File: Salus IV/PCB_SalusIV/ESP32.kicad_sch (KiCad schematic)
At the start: 6 parts

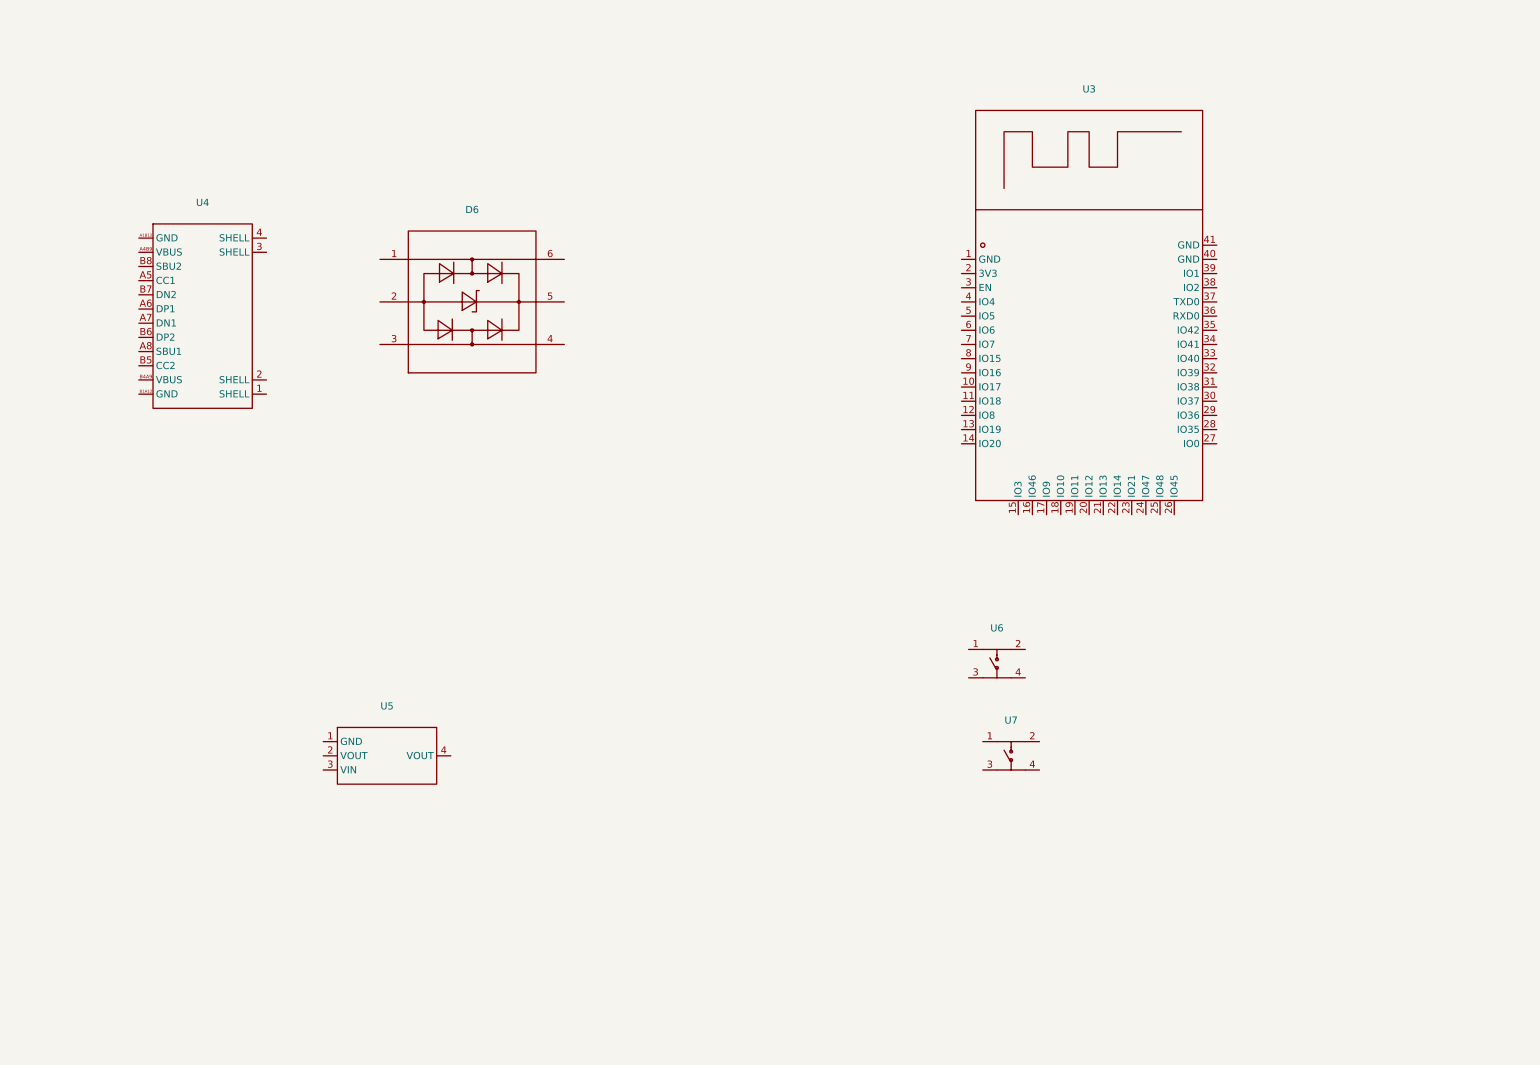
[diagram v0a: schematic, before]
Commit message: Se desarrollo el esquematico de la ESP32
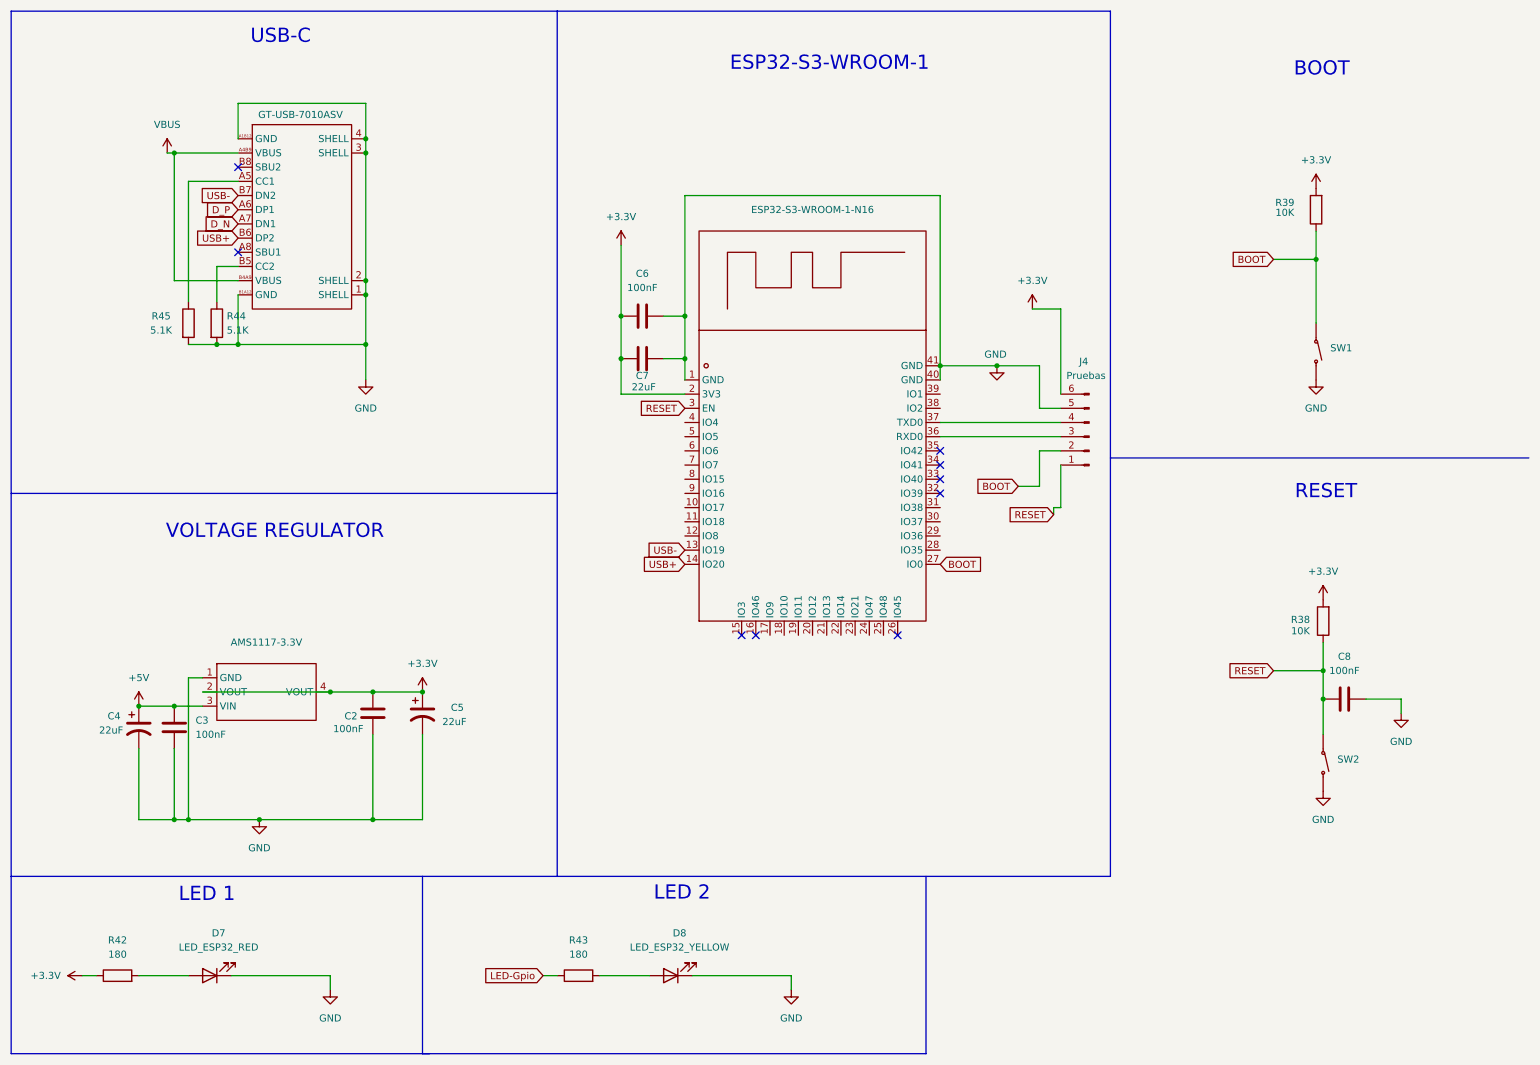
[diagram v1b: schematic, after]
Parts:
- removed D6: ~, Footprints:Protector-ESD, symbol Simbolos:USBLC6-2SC6
- removed U6, U7: ~, Footprints:Switch-Definitivo, symbol Simbolos:TPS645-5NC60
- added C2, C3, C6, C8: 100nF, Capacitor_SMD:C_0402_1005Metric, symbol Device:C
- added C4, C5: 22uF, Footprints:CASE-A_3216, symbol Device:C_Polarized_US
- added C7: 22uF, Capacitor_SMD:C_0402_1005Metric, symbol Device:C
- added D7: LED_ESP32_RED, LED_SMD:LED_0603_1608Metric, symbol Device:LED
- added D8: LED_ESP32_YELLOW, LED_SMD:LED_0603_1608Metric, symbol Device:LED
- added J4: Pruebas, Connector_PinHeader_2.54mm:PinHeader_1x06_P2.54mm_Vertical, symbol Connector:Conn_01x06_Pin
- added R38, R39: 10K, Resistor_SMD:R_1206_3216Metric, symbol Device:R
- added R42, R43: 180, Resistor_SMD:R_1206_3216Metric, symbol Device:R
- added R44, R45: 5.1K, Resistor_SMD:R_1206_3216Metric, symbol Device:R
- added SW1, SW2: ~, Footprints:Boton_Simple, symbol Simbolos:TS1201-TZ25HAM
- renumbered U5 to AMS1117-3.3V, U3 to ESP32-S3-WROOM-1-N16, U4 to GT-USB-7010ASV
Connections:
- net GND: now reaches GT-USB-7010ASV.1 (SHELL)
- net GND: now also AMS1117-3.3V.1 (GND), ESP32-S3-WROOM-1-N16.1 (GND), ESP32-S3-WROOM-1-N16.40 (GND), ESP32-S3-WROOM-1-N16.41 (GND), GT-USB-7010ASV.2 (SHELL), GT-USB-7010ASV.3 (SHELL), GT-USB-7010ASV.4 (SHELL), GT-USB-7010ASV.A1B12 (GND), GT-USB-7010ASV.B1A12 (GND), C2.2, C3.2, C4.2, C5.2, C6.2, C7.2, C8.2, D7.1 (K), D8.1 (K), J4.5 (Pin_5), R44.2, R45.2, SW1.2, SW2.2
- net VBUS: now reaches GT-USB-7010ASV.A4B9 (VBUS)
- net VBUS: now also GT-USB-7010ASV.B4A9 (VBUS)
- net at GT-USB-7010ASV.A5 (CC1): now also R45.1
- net D_P: now reaches GT-USB-7010ASV.A6 (DP1)
- net D_N: now reaches GT-USB-7010ASV.A7 (DN1)
- net at GT-USB-7010ASV.B5 (CC2): now also R44.1
- net USB+: now reaches GT-USB-7010ASV.B6 (DP2)
- net USB+: now also ESP32-S3-WROOM-1-N16.14 (IO20)
- net USB-: now reaches GT-USB-7010ASV.B7 (DN2)
- net USB-: now also ESP32-S3-WROOM-1-N16.13 (IO19)
- net +3.3V: now reaches ESP32-S3-WROOM-1-N16.2 (3V3)
- net +3.3V: now also AMS1117-3.3V.2 (VOUT), AMS1117-3.3V.4 (VOUT), C2.1, C5.1, C6.1, C7.1, J4.6 (Pin_6), R38.2, R39.2, R42.1
- net BOOT: now reaches ESP32-S3-WROOM-1-N16.27 (IO0)
- net BOOT: now also J4.2 (Pin_2), R39.1, SW1.1
- net RESET: now reaches ESP32-S3-WROOM-1-N16.3 (EN)
- net RESET: now also C8.1, J4.1 (Pin_1), R38.1, SW2.1
- net at ESP32-S3-WROOM-1-N16.36 (RXD0): now also J4.3 (Pin_3)
- net at ESP32-S3-WROOM-1-N16.37 (TXD0): now also J4.4 (Pin_4)
- net +5V: now reaches AMS1117-3.3V.3 (VIN)
- net +5V: now also C3.1, C4.1
- new net: D8.2 (A), R43.2
- new net: D7.2 (A), R42.2
- new net LED-Gpio: R43.1
- no-connect marks 0 -> 9
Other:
- note added: "BOOT"
- note added: "ESP32-S3-WROOM-1"
- note added: "LED 1"
- note added: "LED 2"
- note added: "RESET"
- note added: "USB-C"
- note added: "VOLTAGE REGULATOR"
- moved on the sheet: AMS1117-3.3V, ESP32-S3-WROOM-1-N16, GT-USB-7010ASV

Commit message: Se agregan cambios antes de agregar arrays
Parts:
- added J5: GPIO1-Libre, Connector_PinHeader_2.54mm:PinHeader_1x03_P2.54mm_Vertical, symbol Connector:Conn_01x03_Pin
- added J6: GPIO2-Libre, Connector_PinHeader_2.54mm:PinHeader_1x03_P2.54mm_Vertical, symbol Connector:Conn_01x03_Pin
- renumbered AMS1117-3.3V to AMS1117-3.3V1, GT-USB-7010ASV to GT-USB-7010ASV1
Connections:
- net D_N is gone; now on net USB-: GT-USB-7010ASV1.A7 (DN1)
- net D_P is gone; now on net USB+: GT-USB-7010ASV1.A6 (DP1)
- net +3.3V: now also J4.1 (Pin_1); no longer J4.6 (Pin_6)
- net +5V: now also J5.2 (Pin_2), J6.2 (Pin_2)
- net BOOT: now also J4.5 (Pin_5); no longer J4.2 (Pin_2)
- net GND: now also J4.6 (Pin_6), J5.1 (Pin_1), J6.1 (Pin_1); no longer J4.5 (Pin_5)
- net LED-Gpio: now also ESP32-S3-WROOM-1-N16.28 (IO35)
- net RESET: now also J4.2 (Pin_2); no longer J4.1 (Pin_1)
- net TX1: now reaches ESP32-S3-WROOM-1-N16.10 (IO17)
- net RX1: now reaches ESP32-S3-WROOM-1-N16.11 (IO18)
- net PPM: now reaches ESP32-S3-WROOM-1-N16.12 (IO8)
- net HALL-1: now reaches ESP32-S3-WROOM-1-N16.17 (IO9)
- net HALL-2: now reaches ESP32-S3-WROOM-1-N16.18 (IO10)
- net HALL-3: now reaches ESP32-S3-WROOM-1-N16.19 (IO11)
- net ENABLE: now reaches ESP32-S3-WROOM-1-N16.20 (IO12)
- net LPWM: now reaches ESP32-S3-WROOM-1-N16.21 (IO13)
- net RPWM: now reaches ESP32-S3-WROOM-1-N16.22 (IO14)
- net Servo2: now reaches ESP32-S3-WROOM-1-N16.23 (IO21)
- net Servo1: now reaches ESP32-S3-WROOM-1-N16.24 (IO47)
- net ACELERADOR: now reaches ESP32-S3-WROOM-1-N16.25 (IO48)
- net Cambio: now reaches ESP32-S3-WROOM-1-N16.29 (IO36)
- net Reversa: now reaches ESP32-S3-WROOM-1-N16.30 (IO37)
- net Arranque: now reaches ESP32-S3-WROOM-1-N16.31 (IO38)
- net GPIO2: now reaches ESP32-S3-WROOM-1-N16.38 (IO2)
- net GPIO2: now also J5.3 (Pin_3)
- net GPIO1: now reaches ESP32-S3-WROOM-1-N16.39 (IO1)
- net GPIO1: now also J6.3 (Pin_3)
- net SDA_Expansor: now reaches ESP32-S3-WROOM-1-N16.4 (IO4)
- net SCL_Expansor: now reaches ESP32-S3-WROOM-1-N16.5 (IO5)
- net SDA-MUX: now reaches ESP32-S3-WROOM-1-N16.6 (IO6)
- net SCL-MUX: now reaches ESP32-S3-WROOM-1-N16.7 (IO7)
- net ADC_ES: now reaches ESP32-S3-WROOM-1-N16.8 (IO15)
- net Control_Bat: now reaches ESP32-S3-WROOM-1-N16.9 (IO16)

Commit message: Se agrega terminada antes de modificaciones de mejora
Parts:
- added R16, R17: 4.7K, Resistor_SMD:R_1206_3216Metric, symbol Device:R
- C2, C3, C6, C8: footprint Capacitor_SMD:C_0402_1005Metric -> Capacitor_SMD:C_0603_1608Metric; LCSC PN C1525 -> C1590
- C7: footprint Capacitor_SMD:C_0402_1005Metric -> Capacitor_SMD:C_1206_3216Metric
- R44: LCSC PN (none) -> C26044
- U1: renamed from ESP32-S3-WROOM-1-N16; value ~ -> ESP32-S3-WROOM-1-N16
- U4: renamed from AMS1117-3.3V1; value ~ -> AMS
- renumbered GT-USB-7010ASV1 to J21
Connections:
- net +3.3V: now also R16.2, R17.2
- net ENABLE: now also U1.22 (IO14); no longer U1.20 (IO12)
- net RPWM: now also U1.20 (IO12); no longer U1.22 (IO14)
- net SCL-MUX: no longer names the net of U1.7 (IO7)
- net SCL_Expansor renamed SCL-Expansores
- net SCL-Expansores: now also R17.1
- net SDA-MUX: no longer names the net of U1.6 (IO6)
- net SDA_Expansor renamed SDA-Expansores
- net SDA-Expansores: now also R16.1
- no-connect marks 9 -> 11

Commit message: Se guarda la PCB Salus IV ya terminada, queda revision final antes de envio
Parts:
- removed J4: Pruebas, Connector_PinHeader_2.54mm:PinHeader_1x06_P2.54mm_Vertical, symbol Connector:Conn_01x06_Pin
- removed J5: GPIO1-Libre, Connector_PinHeader_2.54mm:PinHeader_1x03_P2.54mm_Vertical, symbol Connector:Conn_01x03_Pin
- removed J6: GPIO2-Libre, Connector_PinHeader_2.54mm:PinHeader_1x03_P2.54mm_Vertical, symbol Connector:Conn_01x03_Pin
- removed R38, R39: 10K, Resistor_SMD:R_1206_3216Metric, symbol Device:R
- removed R43: 180, Resistor_SMD:R_1206_3216Metric, symbol Device:R
- removed R44: 5.1K, Resistor_SMD:R_1206_3216Metric, symbol Device:R
- added J17: Pruebas, Connector_PinHeader_2.54mm:PinHeader_1x06_P2.54mm_Vertical, symbol Connector:Conn_01x06_Pin
- added J18: GPIO2-Libre, Connector_PinHeader_2.54mm:PinHeader_1x03_P2.54mm_Vertical, symbol Connector:Conn_01x03_Pin
- added J19: GPIO1-Libre, Connector_PinHeader_2.54mm:PinHeader_1x03_P2.54mm_Vertical, symbol Connector:Conn_01x03_Pin
- added R22, R23: 10K, Resistor_SMD:R_0603_1608Metric, symbol Device:R
- added R24: 180, Resistor_SMD:R_0603_1608Metric, symbol Device:R
- added R25: 5.1K, Resistor_SMD:R_0603_1608Metric, symbol Device:R
- R16, R17: footprint Resistor_SMD:R_1206_3216Metric -> Resistor_SMD:R_0603_1608Metric; LCSC PN C26043 -> C99782
- R27: renamed from R42; footprint Resistor_SMD:R_1206_3216Metric -> Resistor_SMD:R_0603_1608Metric; LCSC PN C25356 -> C4316945
- R28: renamed from R45; footprint Resistor_SMD:R_1206_3216Metric -> Resistor_SMD:R_0603_1608Metric; LCSC PN C26044 -> C14677
- renumbered J21 to J16
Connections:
- net +3.3V: now also R16.1, R17.1, J17.1 (Pin_1), R22.2, R23.2; no longer R16.2, R17.2
- net +5V: now also J18.2 (Pin_2), J19.2 (Pin_2)
- net BOOT: now also J17.5 (Pin_5), R23.1
- net GND: now also J17.6 (Pin_6), J18.1 (Pin_1), J19.1 (Pin_1), R25.2
- net GPIO1: now also J18.3 (Pin_3)
- net GPIO2: now also J19.3 (Pin_3)
- net LED-Gpio: now also R24.1
- net RESET: now also J17.2 (Pin_2), R22.1
- net SCL-Expansores: now also R16.2; no longer R17.1
- net SDA-Expansores: now also R17.2; no longer R16.1
- net at J16.B5 (CC2): now also R25.1
- net at D8.2 (A): now also R24.2
- net at U1.36 (RXD0): now also J17.3 (Pin_3)
- net at U1.37 (TXD0): now also J17.4 (Pin_4)
- net SDA-Giro: now reaches U1.6 (IO6)
- net SCL-Giro: now reaches U1.7 (IO7)
- no-connect marks 11 -> 9
